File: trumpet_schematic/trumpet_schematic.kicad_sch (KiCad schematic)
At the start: 5 parts, among them J1 LCD, Q1 NPN

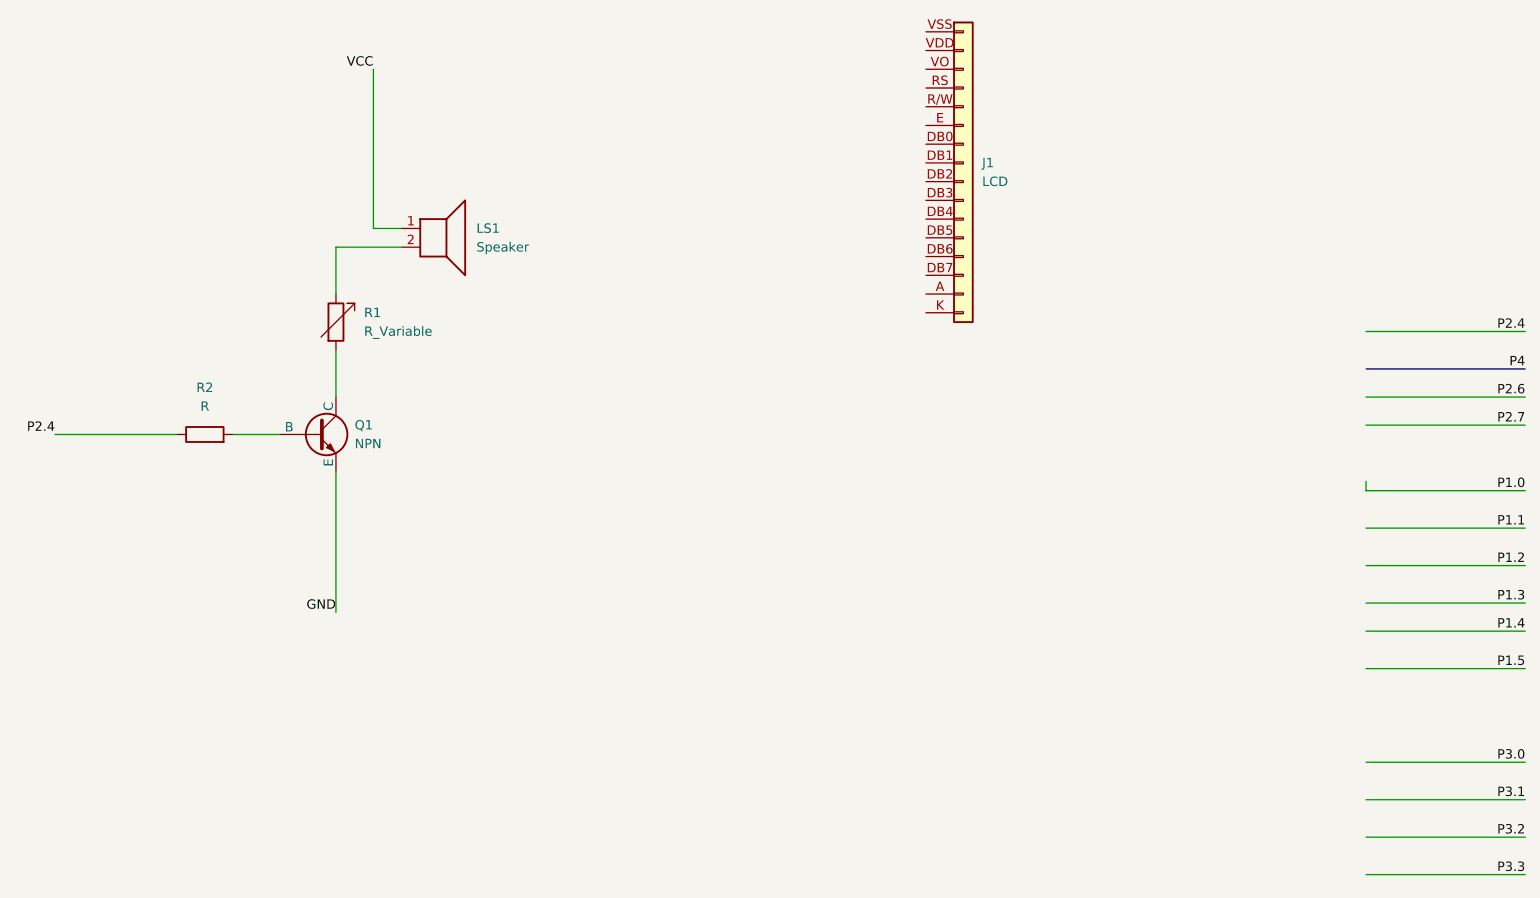
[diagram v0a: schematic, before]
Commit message: schematic done
schematic for final project drawn
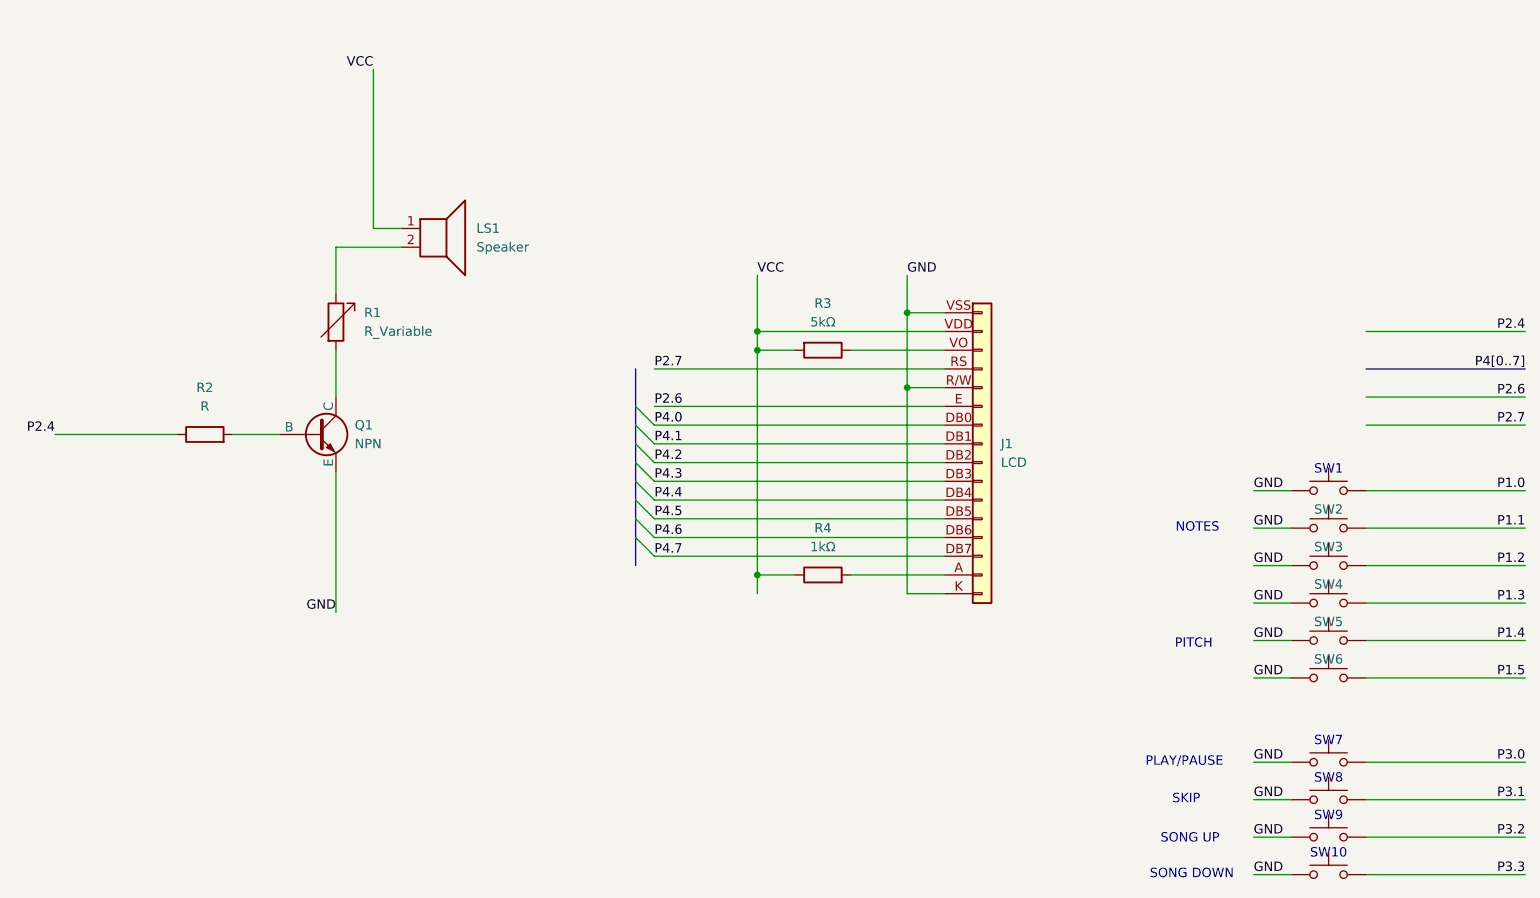
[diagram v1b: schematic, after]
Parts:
- added R3: 5kΩ, symbol Device:R
- added R4: 1kΩ, symbol Device:R
- added SW1, SW10, SW2, SW3, SW4, SW5, SW6, SW7, SW8, SW9: SW_Push, symbol Switch:SW_Push
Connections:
- net GND: now also J1.K (16), J1.R/W (Pin_5), J1.VSS (1), SW1.1, SW10.1, SW2.1, SW3.1, SW4.1, SW5.1, SW6.1, SW7.1, SW8.1, SW9.1
- net P1.0: now also SW1.2
- net P1.1: now also SW2.2
- net P1.2: now also SW3.2
- net P1.3: now also SW4.2
- net P1.4: now also SW5.2
- net P1.5: now also SW6.2
- net P2.6: now also J1.E (6)
- net P2.7: now also J1.RS (4)
- net P3.0: now also SW7.2
- net P3.1: now also SW8.2
- net P3.2: now also SW9.2
- net P3.3: now also SW10.2
- net VCC: now also J1.VDD (Pin_2), R3.2, R4.1
- net at J1.A (15): now also R4.2
- net P4.0: now reaches J1.DB0 (Pin_7)
- net P4.1: now reaches J1.DB1 (Pin_8)
- net P4.2: now reaches J1.DB2 (Pin_9)
- net P4.3: now reaches J1.DB3 (10)
- net P4.4: now reaches J1.DB4 (11)
- net P4.5: now reaches J1.DB5 (Pin_12)
- net P4.6: now reaches J1.DB6 (Pin_13)
- net P4.7: now reaches J1.DB7 (Pin_14)
- net at J1.VO (Pin_3): now also R3.1
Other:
- note added: "NOTES"
- note added: "PITCH"
- note added: "PLAY/PAUSE"
- note added: "SKIP"
- note added: "SONG DOWN"
- note added: "SONG UP"
- note added: "SW1"
- note added: "SW10"
- note added: "SW7"
- note added: "SW8"
- note added: "SW9"
- company: (none) -> Rose-Hulman Institute of Technology
- title: (none) -> Trumpet Schematic
- moved on the sheet: J1
